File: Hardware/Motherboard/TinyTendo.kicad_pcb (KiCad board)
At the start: 4 copper layers, 64.7 x 52.2 mm, 48 parts, among them J1 Conn_01x01_Male, J2 Conn_01x01_Male, J3 Conn_01x01_Male, J4 Conn_01x01_Male, J5 Conn_01x01_Male, J6 Conn_01x01_Male, J7 Conn_01x01_Male, J8 Conn_01x01_Male, J9 Conn_01x01_Male, P1 72-Pin Connector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

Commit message: + Fixed error on InCU1 layer + Added missing pads for audio amp power + Removed redundant autosave files
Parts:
- added J2: Conn_01x01_Male, TinyTendo:SolderPad, F.Cu at (234.1, 117.8)
- added J6: Conn_01x01_Male, TinyTendo:SolderPad, F.Cu at (232.1, 116.3)
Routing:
- net /PPU-A4: track 54.1 -> 53.6 mm
- net /VCC: vias 17 -> 18
- net /GND: vias 23 -> 32

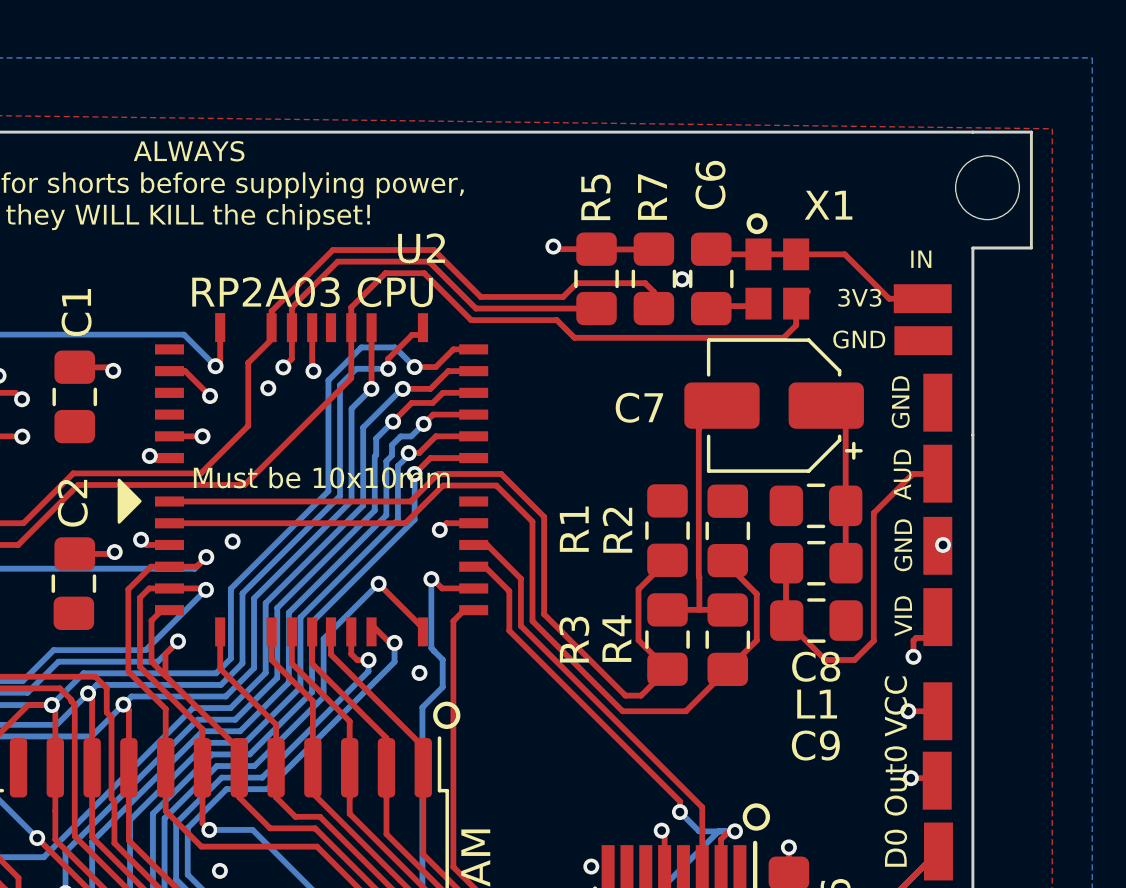
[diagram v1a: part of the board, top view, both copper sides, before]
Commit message: +Update Motherboard to use more available SiT2001B oscillator.
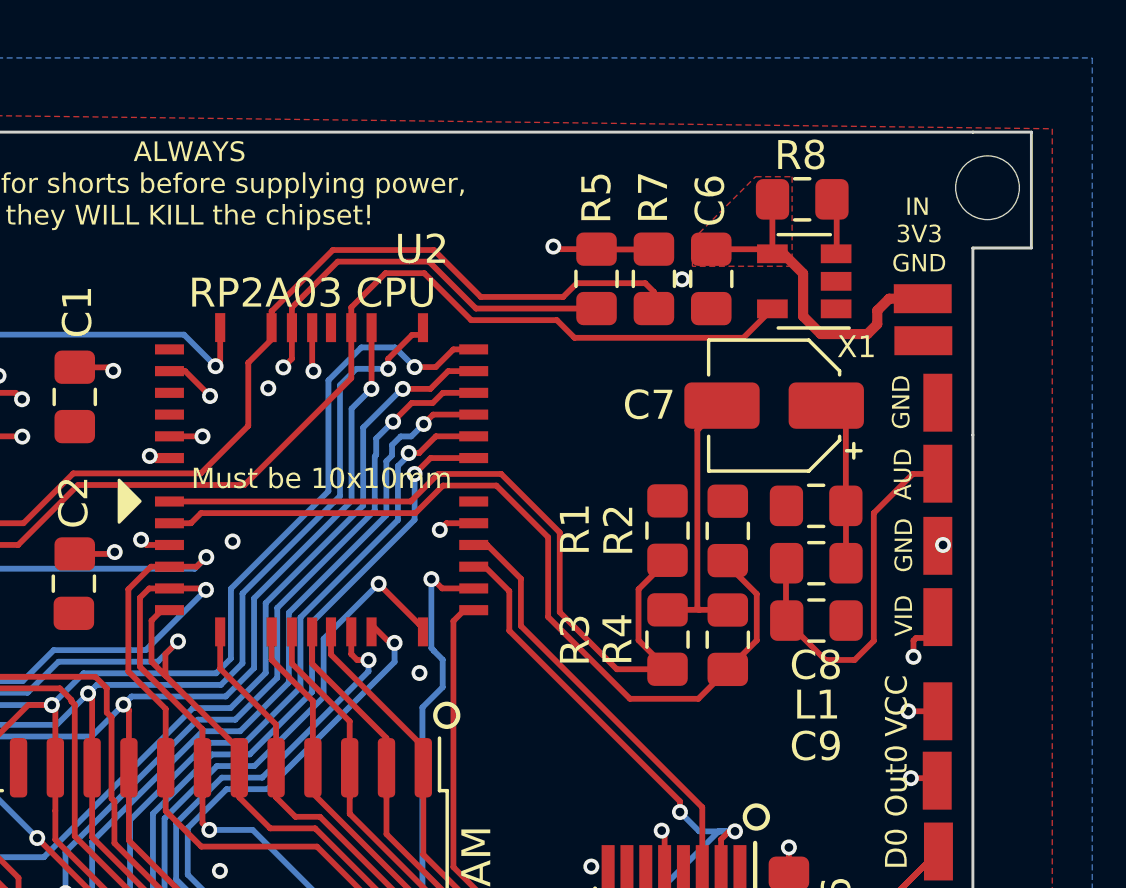
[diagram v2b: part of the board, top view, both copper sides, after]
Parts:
- added R8: 1K, Resistor_SMD:R_0805_2012Metric_Pad1.15x1.40mm_HandSolder, F.Cu at (229.9, 80.9)
- C3, C9: value 10nF -> 0.1uF
- L1: value 39u -> 39uH
- X1: value SG-8018CG-TJHPAB -> SiT2001B; footprint TinyTendo:Oscillator -> Package_TO_SOT_SMD:SOT-23-5
- moved X1 0.97 mm to (229.9, 83.8), turned to 180 degrees
- turned C6 to 90 degrees
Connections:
- C6 pad 1: /3V3 -> /GND
- C6 pad 2: /GND -> /3V3
- X1 pad 1: /3V3 -> /GND
- X1 pad 2: /GND -> Net-(X1-Pad2)
- X1 pad 3: /SYS-CLK -> Net-(R8-Pad1)
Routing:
- net /3V3: track 8.01 -> 12.3 mm
- net Net-(R8-Pad1): track 0.00 -> 1.96 mm
- net /SYS-CLK: track 36.1 -> 34.2 mm
- net /GND: track 20.1 -> 18.4 mm
- net /OUT-0: track 38.5 -> 39.8 mm
- net /SOUND-1: track 27.4 -> 26.3 mm
- net Net-(C7-Pad1): track 5.72 -> 6.68 mm
- net /SOUND-2: track 30.0 -> 29.2 mm
- added copper zone on F.Cu, net /3V3
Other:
- board text added: "No Emulation, No Exceptions"
